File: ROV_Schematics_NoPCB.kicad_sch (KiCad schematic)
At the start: 7 parts

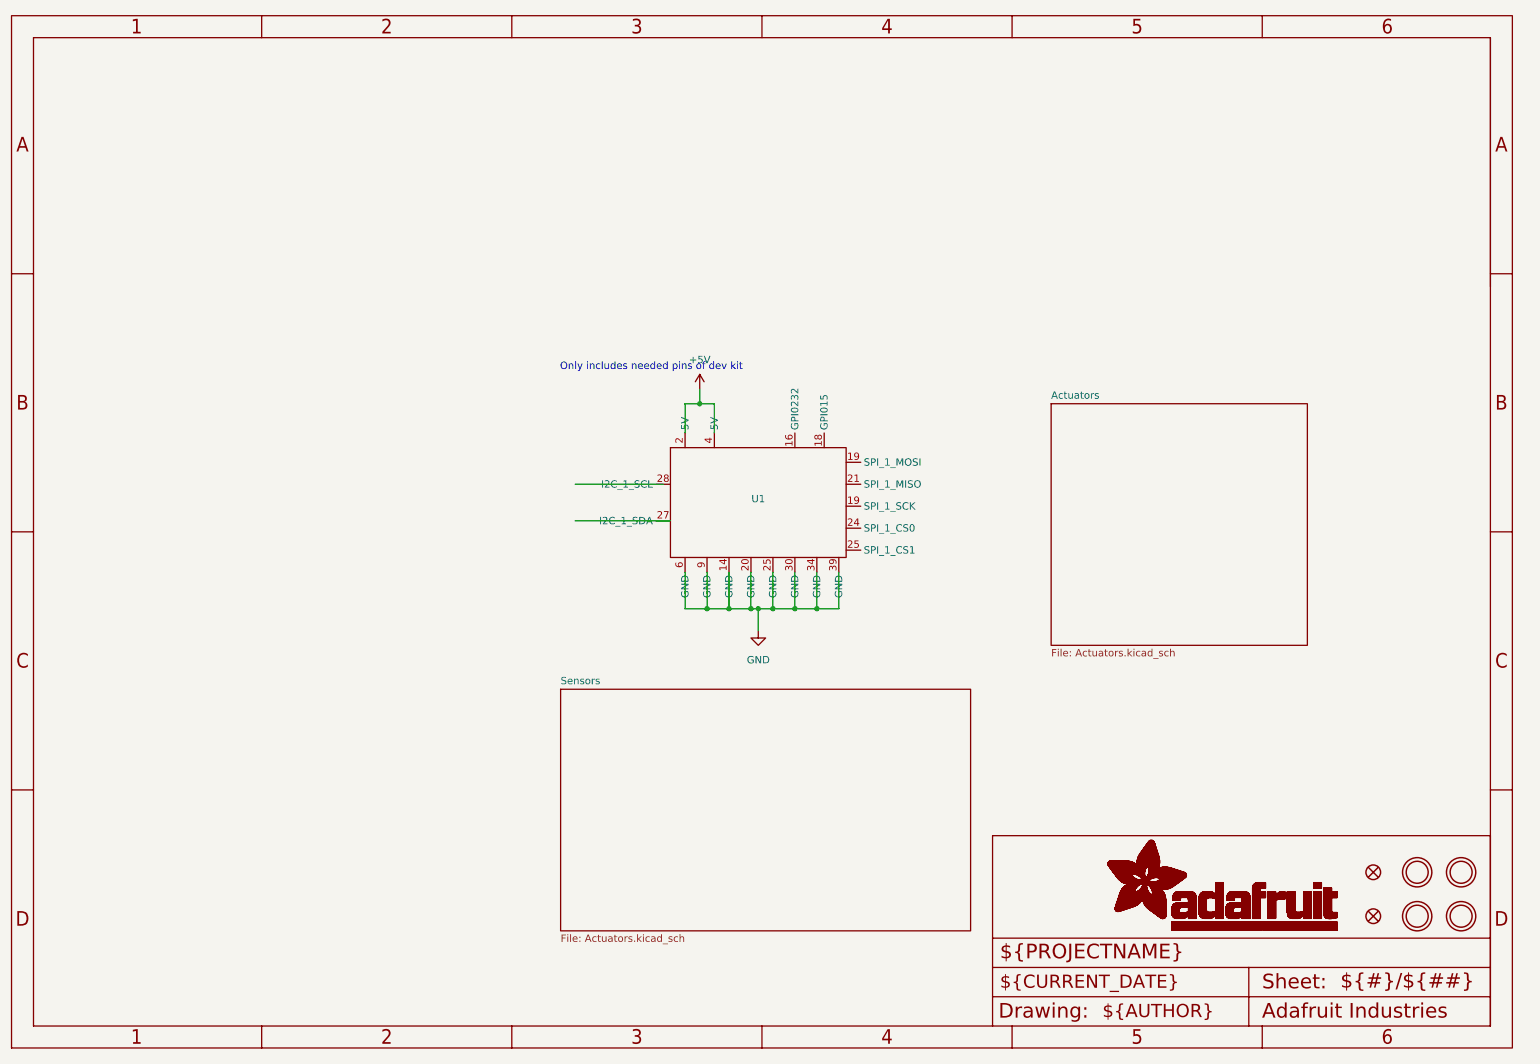
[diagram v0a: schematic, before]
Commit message: Added Thruster and ESC symbols
Added Thruster and ESC symbols
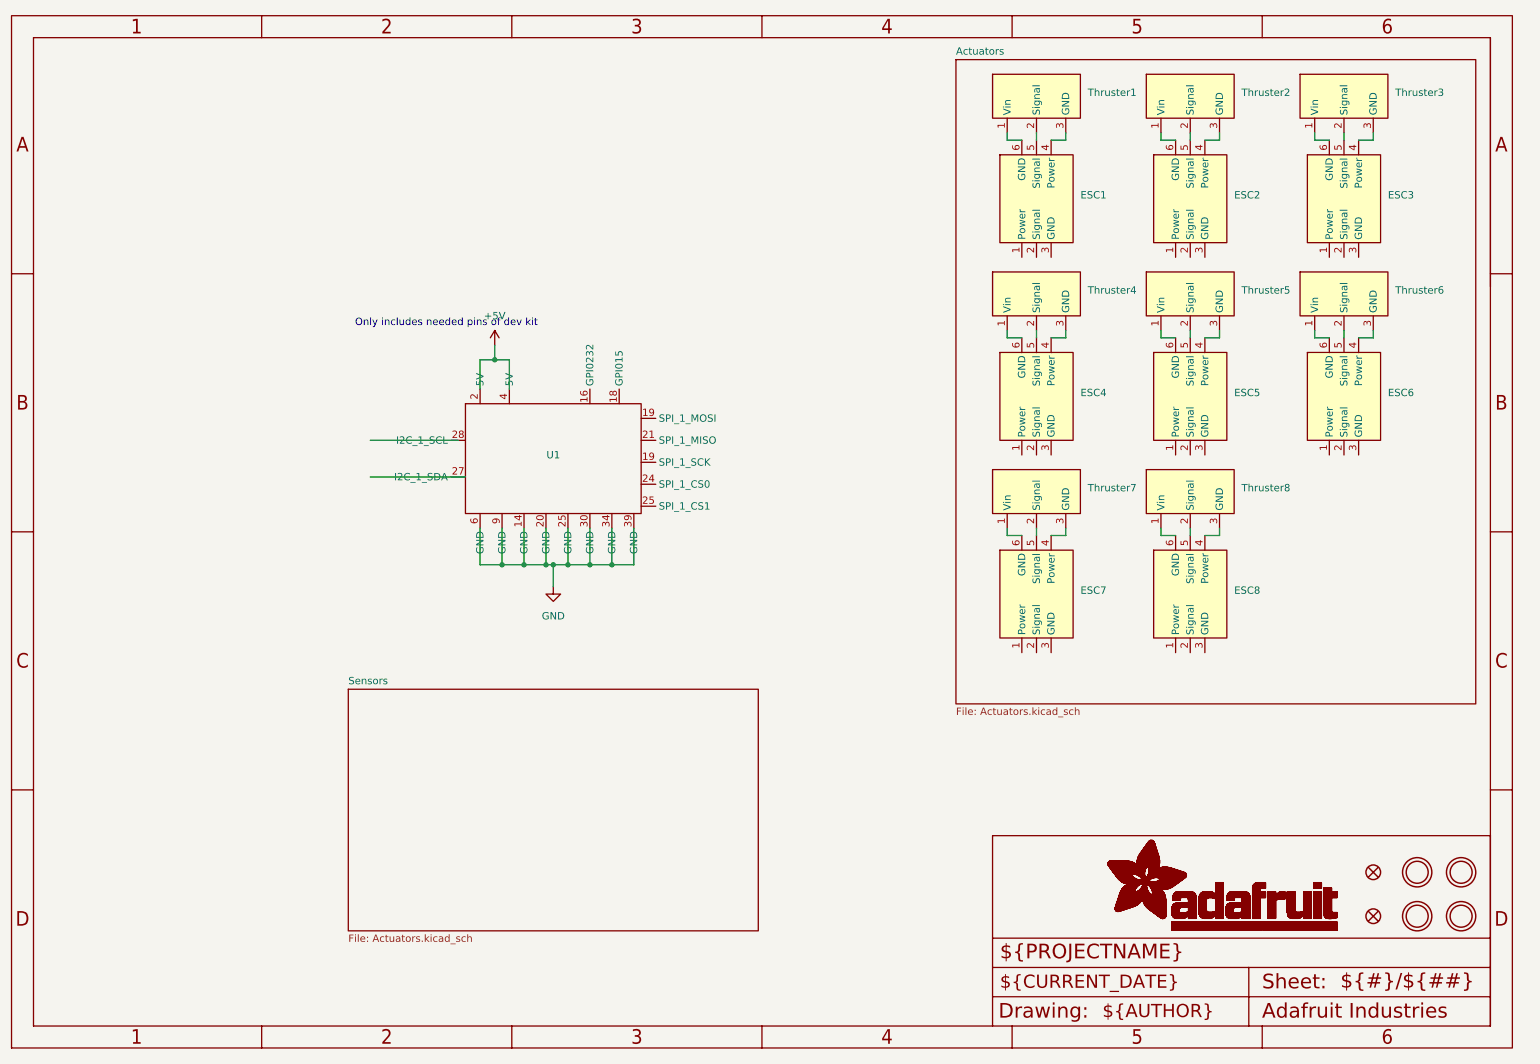
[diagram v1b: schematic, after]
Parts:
- added ESC1, ESC2, ESC3, ESC4, ESC5, ESC6, ESC7, ESC8: ~, symbol ROV_Custom_Symbols:Thruster_ESC
- added Thruster1, Thruster2, Thruster3, Thruster4, Thruster5, Thruster6, Thruster7, Thruster8: ~, symbol ROV_Custom_Symbols:Thruster
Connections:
- new net: ESC3.6 (GND), Thruster3.1 (Vin)
- new net: ESC3.5 (Signal), Thruster3.2 (Signal)
- new net: ESC3.4 (Power), Thruster3.3 (GND)
- new net: ESC6.4 (Power), Thruster6.3 (GND)
- new net: ESC6.5 (Signal), Thruster6.2 (Signal)
- new net: ESC6.6 (GND), Thruster6.1 (Vin)
- new net: ESC8.4 (Power), Thruster8.3 (GND)
- new net: ESC8.5 (Signal), Thruster8.2 (Signal)
- new net: ESC8.6 (GND), Thruster8.1 (Vin)
- new net: ESC4.6 (GND), Thruster4.1 (Vin)
- new net: ESC4.5 (Signal), Thruster4.2 (Signal)
- new net: ESC4.4 (Power), Thruster4.3 (GND)
- new net: ESC7.6 (GND), Thruster7.1 (Vin)
- new net: ESC7.5 (Signal), Thruster7.2 (Signal)
- new net: ESC7.4 (Power), Thruster7.3 (GND)
- new net: ESC1.6 (GND), Thruster1.1 (Vin)
- new net: ESC1.5 (Signal), Thruster1.2 (Signal)
- new net: ESC1.4 (Power), Thruster1.3 (GND)
- new net: ESC5.6 (GND), Thruster5.1 (Vin)
- new net: ESC5.5 (Signal), Thruster5.2 (Signal)
- new net: ESC5.4 (Power), Thruster5.3 (GND)
- new net: ESC2.4 (Power), Thruster2.3 (GND)
- new net: ESC2.5 (Signal), Thruster2.2 (Signal)
- new net: ESC2.6 (GND), Thruster2.1 (Vin)
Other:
- moved on the sheet: U1

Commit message: Added temperature and leak sensors
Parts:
- added U10: ~, symbol ROV_Custom_Symbols:SEN0454
- added U8: TMP36xS, Package_SO:SOIC-8_3.9x4.9mm_P1.27mm, symbol Sensor_Temperature:TMP36xS
- added U9: ~, symbol ROV_Custom_Symbols:SOS_Leak_Sensor
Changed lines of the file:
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@@
 			)
 		)
-		(property "Description" ""
+		(property "Description" "Mounting Hole\n\nFor #2 screws (0.086\"/2.18mm width, 0.094\"/2.4mm hole) use 2.5mm"
 			(at 269.24 175.26 0)
 			(effects
@@
 			)
 		)
-		(property "Description" ""
+		(property "Description" "Fiducial Alignment Points\n\nVarious fiducial points for machine vision alignment."
 			(at 254 167.64 0)
 			(effects
@@
 	)
 	(symbol
+		(lib_id "ROV_Custom_Symbols:SOS_Leak_Sensor")
+		(at 124.46 151.13 0)
+		(unit 1)
+		(exclude_from_sim no)
+		(in_bom yes)
+		(on_board yes)
+		(dnp no)
+		(property "Reference" "U9"
+			(at 134.62 145.288 0)
+			(effects
+				(font
+					(size 1.27 1.27)
+				)
+				(justify left)
+			)
+		)
+		(property "Value" "~"
+			(at 142.24 152.4 0)
+			(effects
+				(font
+					(size 1.27 1.27)
+				)
+				(justify left)
+			)
+		)
+		(property "Footprint" ""
+			(at 124.46 151.13 0)
+			(effects
+				(font
+					(size 1.27 1.27)
+				)
+				(hide yes)
+			)
+		)
+		(property "Datasheet" ""
+			(at 124.46 151.13 0)
+			(effects
+				(font
+					(size 1.27 1.27)
+				)
+				(hide yes)
+			)
+		)
+		(property "Description" ""
+			(at 124.46 151.13 0)
+			(effects
+				(font
+					(size 1.27 1.27)
+				)
+				(hide yes)
+			)
+		)
+		(pin ""
+		)
+		(pin ""
+		)
+		(pin ""
+		)
+		(instances
+			(project "ROV_Schematics_NoPCB"
+				(path "/01af68dd-14ea-43f3-adc5-e1905c3175ab"
+					(reference "U9")
+					(unit 1)
+				)
+			)
+		)
+	)
+	(symbol
 		(lib_id "ROV_Custom_Symbols:Thruster")
 		(at 195.58 107.95 0)
@@
 	)
 	(symbol
+		(lib_id "Sensor_Temperature:TMP36xS")
+		(at 88.9 149.86 0)
+		(unit 1)
+		(exclude_from_sim no)
+		(in_bom yes)
+		(on_board yes)
+		(dnp no)
+		(fields_autoplaced yes)
+		(property "Reference" "U8"
+			(at 104.14 143.5414 0)
+			(effects
+				(font
+					(size 1.27 1.27)
+				)
+			)
+		)
+		(property "Value" "TMP36xS"
+			(at 104.14 146.0814 0)
+			(effects
+				(font
+					(size 1.27 1.27)
+				)
+			)
+		)
+		(property "Footprint" "Package_SO:SOIC-8_3.9x4.9mm_P1.27mm"
+			(at 88.9 161.29 0)
+			(effects
+				(font
+					(size 1.27 1.27)
+				)
+				(hide yes)
+			)
+		)
+		(property "Datasheet" "https://www.analog.com/media/en/technical-documentation/data-sheets/TMP35_36_37.pdf"
+			(at 88.9 149.86 0)
+			(effects
+				(font
+					(size 1.27 1.27)
+				)
+				(hide yes)
+			)
+		)
+		(property "Description" "Low Voltage Temperature Sensor, SOIC-8"
+			(at 88.9 149.86 0)
+			(effects
+				(font
+					(size 1.27 1.27)
+				)
+				(hide yes)
+			)
+		)
+		(pin "8"
+		)
+		(pin "4"
+		)
+		(pin "1"
+		)
+		(pin "5"
+		)
+		(instances
+			(project "ROV_Schematics_NoPCB"
+				(path "/01af68dd-14ea-43f3-adc5-e1905c3175ab"
+					(reference "U8")
+					(unit 1)
+				)
+			)
+		)
+	)
+	(symbol
 		(lib_id "ROV_Custom_Symbols:Thruster")
 		(at 195.58 39.37 0)
@@
 			)
 		)
-		(property "Description" ""
+		(property "Description" "Frame A4"
 			(at 17.78 198.12 0)
 			(effects
@@
 			)
 		)
-		(property "Description" ""
+		(property "Description" "Mounting Hole\n\nFor #2 screws (0.086\"/2.18mm width, 0.094\"/2.4mm hole) use 2.5mm"
 			(at 261.62 175.26 0)
 			(effects
@@
 	)
 	(symbol
+		(lib_id "ROV_Custom_Symbols:SEN0454")
+		(at 154.94 149.86 0)
+		(unit 1)
+		(exclude_from_sim no)
+		(in_bom yes)
+		(on_board yes)
+		(dnp no)
+		(property "Reference" "U10"
+			(at 166.878 137.668 0)
+			(effects
+				(font
+					(size 1.27 1.27)
+				)
+				(justify left)
+			)
+		)
+		(property "Value" "~"
+			(at 173.99 151.13 0)
+			(effects
+				(font
+					(size 1.27 1.27)
+				)
+				(justify left)
+			)
+		)
+		(property "Footprint" ""
+			(at 154.94 157.48 0)
+			(effects
+				(font
+					(size 1.27 1.27)
+				)
+				(hide yes)
+			)
+		)
+		(property "Datasheet" ""
+			(at 154.94 157.48 0)
+			(effects
+				(font
+					(size 1.27 1.27)
+				)
+				(hide yes)
+			)
+		)
+		(property "Description" ""
+			(at 154.94 157.48 0)
+			(effects
+				(font
+					(size 1.27 1.27)
+				)
+				(hide yes)
+			)
+		)
+		(pin ""
+		)
+		(pin ""
+		)
+		(pin ""
+		)
+		(pin ""
+		)
+		(pin ""
+		)
+		(instances
+			(project "ROV_Schematics_NoPCB"
+				(path "/01af68dd-14ea-43f3-adc5-e1905c3175ab"
+					(reference "U10")
+					(unit 1)
+				)
+			)
+		)
+	)
+	(symbol
 		(lib_id "power:+5V")
 		(at 101.6 76.2 0)
@@
 			)
 		)
-		(property "Description" ""
+		(property "Description" "Mounting Hole\n\nFor #2 screws (0.086\"/2.18mm width, 0.094\"/2.4mm hole) use 2.5mm"
 			(at 261.62 167.64 0)
 			(effects
@@
 			)
 		)
-		(property "Description" ""
+		(property "Description" "Fiducial Alignment Points\n\nVarious fiducial points for machine vision alignment."
 			(at 254 175.26 0)
 			(effects
@@
 			)
 		)
-		(property "Description" ""
+		(property "Description" "Mounting Hole\n\nFor #2 screws (0.086\"/2.18mm width, 0.094\"/2.4mm hole) use 2.5mm"
 			(at 269.24 167.64 0)
 			(effects
@@
 	)
 	(sheet
-		(at 76.2 135.89)
-		(size 71.12 41.91)
+		(at 73.66 135.89)
+		(size 100.33 53.34)
 		(fields_autoplaced yes)
 		(stroke
@@
 		)
 		(property "Sheetname" "Sensors"
-			(at 76.2 135.1784 0)
+			(at 73.66 135.1784 0)
 			(effects
 				(font
@@
 		)
 		(property "Sheetfile" "Actuators.kicad_sch"
-			(at 76.2 178.3846 0)
-			(effects
-				(font
+			(at 73.66 189.8146 0)
+			(effects
+				(font
